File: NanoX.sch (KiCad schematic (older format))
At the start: 37 parts, among them J1 10118192-0001LF, J2 Conn_ARM_JTAG_SWD_10, J3 Conn_01x11, J4 NanoClassic_R, J5 Conn_01x11, J6 NanoClassic_L, SW1 SW_Push, U1 ATSAMD21G18A-AUT, U2 MCP1725-3302E_MC, U3 CAT24C16YI-GT3

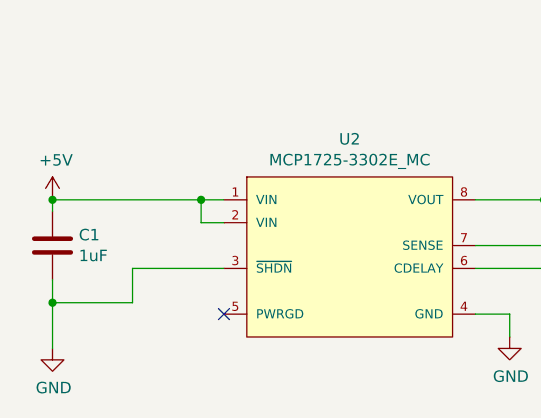
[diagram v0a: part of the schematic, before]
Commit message: Change pin 3 of MCP1725 to Vin instead of GND.
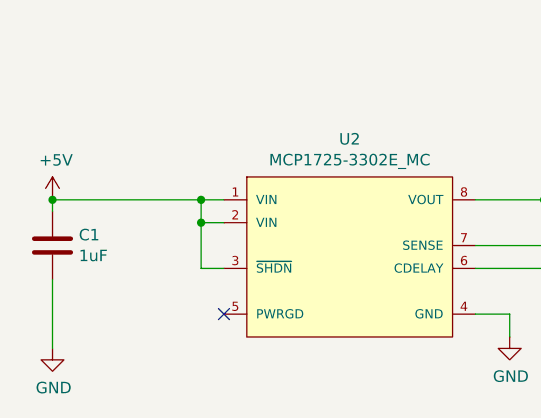
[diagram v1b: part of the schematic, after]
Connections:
- net +5V: now also U2.3 (~SHDN~)
- net GND: no longer U2.3 (~SHDN~)
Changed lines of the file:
@@
 	1    0    0    -1
 $EndComp
-Wire Wire Line
-	950  6150 950  6250
-Wire Wire Line
-	1700 6100 1300 6100
-Wire Wire Line
-	1300 6100 1300 6250
-Wire Wire Line
-	1300 6250 950  6250
-Connection ~ 950  6250
-Wire Wire Line
-	950  6250 950  6450
 NoConn ~ 1700 6300
 $Comp
@@
 Wire Wire Line
 	8850 2200 8750 2200
-Wire Bus Line
-	7450 4600 7450 6350
-Wire Bus Line
-	5150 1750 5150 4600
-Wire Bus Line
-	10600 1750 10600 6350
-Wire Bus Line
-	7450 1700 7450 4600
 $Comp
 L switches:SW_Push SW1
@@
 	-1   0    0    -1
 $EndComp
+Wire Wire Line
+	950  6150 950  6450
+Wire Wire Line
+	1700 6100 1600 6100
+Wire Wire Line
+	1600 6100 1600 5900
+Wire Bus Line
+	7450 4600 7450 6350
+Wire Bus Line
+	5150 1750 5150 4600
+Wire Bus Line
+	10600 1750 10600 6350
+Wire Bus Line
+	7450 1700 7450 4600
+Connection ~ 1600 5900
 $EndSCHEMATC
